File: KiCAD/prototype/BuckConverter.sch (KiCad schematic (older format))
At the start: 18 parts

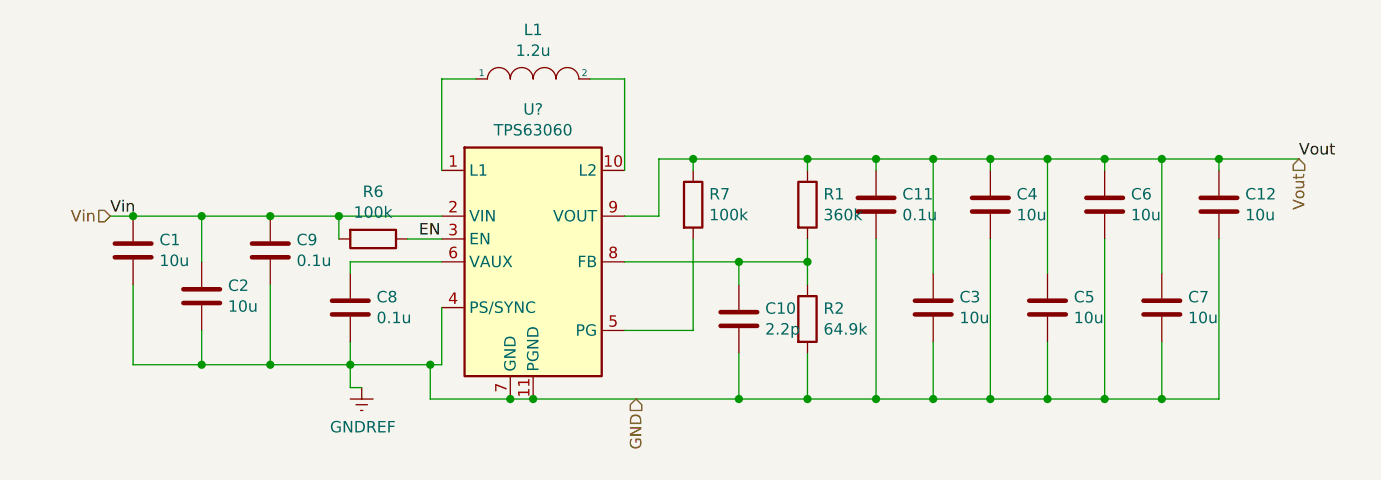
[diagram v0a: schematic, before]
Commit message: Improve BuckConverter schematic readability
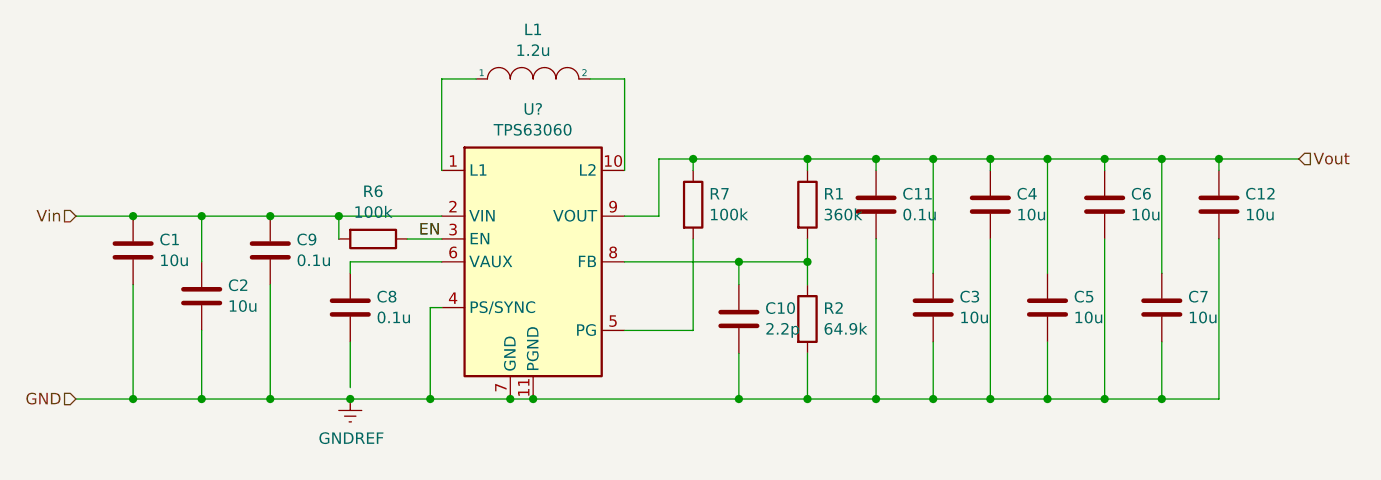
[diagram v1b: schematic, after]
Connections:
- net GNDREF: no longer C8.2
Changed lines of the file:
@@
 Wire Wire Line
 	5900 2800 5900 3200
-Text Label 3650 3400 0    50   ~ 0
-Vin
 $Comp
 L Device:C C2
@@
 L power:GNDREF #PWR?
 U 1 1 5FAC5813
-P 4750 4150
-F 0 "#PWR?" H 4750 3900 50  0001 C CNN
-F 1 "GNDREF" H 4755 3977 50  0000 C CNN
-F 2 "" H 4750 4150 50  0001 C CNN
-F 3 "" H 4750 4150 50  0001 C CNN
-	1    4750 4150
-	1    0    0    -1
-$EndComp
-Wire Wire Line
-	4700 3950 4700 4050
-Wire Wire Line
-	4700 4150 4750 4150
-Wire Wire Line
-	4700 4050 5050 4050
-Wire Wire Line
-	5100 4050 5100 3800
-Connection ~ 4700 4050
-Wire Wire Line
-	4700 4050 4700 4150
-Wire Wire Line
-	5050 4050 5050 4200
+P 4700 4200
+F 0 "#PWR?" H 4700 3950 50  0001 C CNN
+F 1 "GNDREF" H 4705 4027 50  0000 C CNN
+F 2 "" H 4700 4200 50  0001 C CNN
+F 3 "" H 4700 4200 50  0001 C CNN
+	1    4700 4200
+	1    0    0    -1
+$EndComp
 Wire Wire Line
 	5050 4200 5400 4200
-Connection ~ 5050 4050
-Wire Wire Line
-	5050 4050 5100 4050
 $Comp
 L Device:R R6
@@
 Wire Wire Line
 	4650 3400 4350 3400
-Wire Wire Line
-	4050 3900 4050 4050
-Wire Wire Line
-	3750 4050 4050 4050
-Connection ~ 4050 4050
-Wire Wire Line
-	4050 4050 4350 4050
-Wire Wire Line
-	4350 3700 4350 4050
-Connection ~ 4350 4050
-Wire Wire Line
-	4350 4050 4700 4050
 Text Label 5000 3500 0    50   ~ 0
 EN
@@
 	8500 3150 8850 3150
 Connection ~ 8500 3150
-Text Label 8850 3150 0    50   ~ 0
-Vout
 Wire Wire Line
 	5100 3400 4650 3400
-Wire Wire Line
-	3750 3700 3750 4050
 $Comp
 L Device:C C1
@@
 Connection ~ 3750 3400
 Wire Wire Line
-	3750 3400 3650 3400
-Wire Wire Line
 	4050 3600 4050 3400
 Connection ~ 4050 3400
 Wire Wire Line
 	4050 3400 3750 3400
-Text HLabel 3650 3400 0    50   Input ~ 0
+Text HLabel 3500 3400 0    50   Input ~ 0
 Vin
-Text HLabel 8850 3150 3    50   Input ~ 0
+Text HLabel 8850 3150 2    50   Input ~ 0
 Vout
-Text HLabel 5950 4200 3    50   Input ~ 0
+Text HLabel 3500 4200 0    50   Input ~ 0
 GND
+Wire Wire Line
+	4700 4200 5050 4200
+Connection ~ 5050 4200
+Wire Wire Line
+	4700 4200 4350 4200
+Connection ~ 4700 4200
+Wire Wire Line
+	4350 4200 4050 4200
+Connection ~ 4350 4200
+Wire Wire Line
+	4050 4200 3750 4200
+Connection ~ 4050 4200
+Wire Wire Line
+	3750 3700 3750 4200
+Wire Wire Line
+	4050 3900 4050 4200
+Wire Wire Line
+	4350 3700 4350 4200
+Wire Wire Line
+	4700 3950 4700 4150
+Wire Wire Line
+	5050 3800 5100 3800
+Wire Wire Line
+	5050 3800 5050 4200
+Wire Wire Line
+	3500 4200 3750 4200
+Connection ~ 3750 4200
+Wire Wire Line
+	3500 3400 3750 3400
 $EndSCHEMATC

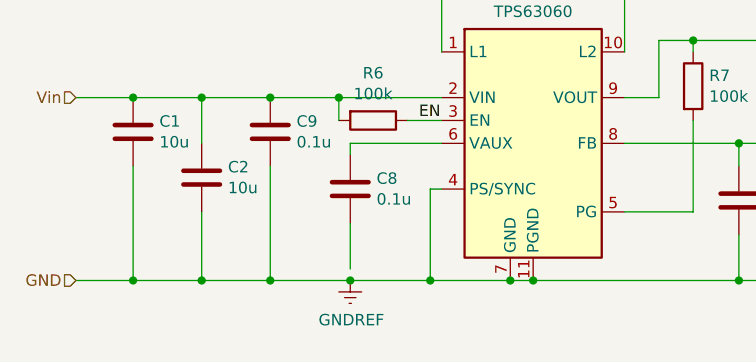
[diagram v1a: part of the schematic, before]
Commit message: Fix unconnected line
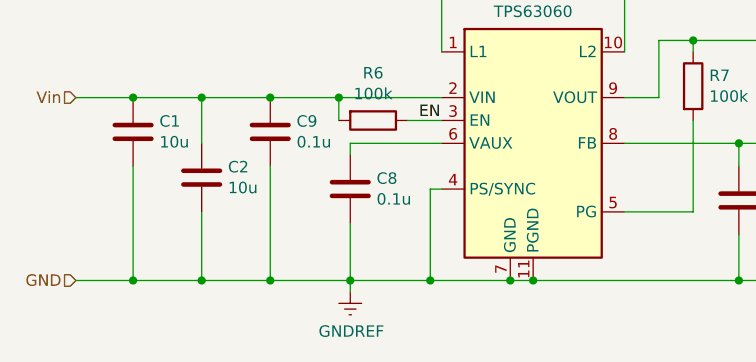
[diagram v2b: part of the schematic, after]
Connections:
- net GNDREF: now also C8.2
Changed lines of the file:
@@
 L power:GNDREF #PWR?
 U 1 1 5FAC5813
-P 4700 4200
-F 0 "#PWR?" H 4700 3950 50  0001 C CNN
-F 1 "GNDREF" H 4705 4027 50  0000 C CNN
-F 2 "" H 4700 4200 50  0001 C CNN
-F 3 "" H 4700 4200 50  0001 C CNN
-	1    4700 4200
+P 4700 4250
+F 0 "#PWR?" H 4700 4000 50  0001 C CNN
+F 1 "GNDREF" H 4705 4077 50  0000 C CNN
+F 2 "" H 4700 4250 50  0001 C CNN
+F 3 "" H 4700 4250 50  0001 C CNN
+	1    4700 4250
 	1    0    0    -1
 $EndComp
@@
 	4350 3700 4350 4200
 Wire Wire Line
-	4700 3950 4700 4150
-Wire Wire Line
 	5050 3800 5100 3800
 Wire Wire Line
@@
 Wire Wire Line
 	3500 3400 3750 3400
+Wire Wire Line
+	4700 3950 4700 4200
+Wire Wire Line
+	4700 4250 4700 4200
 $EndSCHEMATC
